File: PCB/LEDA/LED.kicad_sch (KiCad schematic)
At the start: 25 parts, among them J1 USB_A, J2 Conn_01x03, J3 TC2030-USB-NL-DS, U1 ICS43434_MEMS_Mic, U2 ESP32-S3-MINI-1, U5 MD8942

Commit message: PCB Update
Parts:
- C4, C6: LCSC Part # C194427 -> (none); MPN (none) -> C194427
- C7: LCSC Part # C1691 -> (none); MPN (none) -> C1691
- D1: LCSC Part # C5349953 -> (none); MPN (none) -> C5349953
- D2: LCSC Part # C5137770 -> (none); MPN (none) -> C5137770
- J2: LCSC Part # C2765056 -> (none); MPN (none) -> C2765056
- U1: LCSC Part # C5656610 -> (none); MPN (none) -> C5656610
- U2: LCSC Part # C3013941 -> (none); MPN (none) -> C3013941
- U5: LCSC Part # C2684786 -> (none); MPN (none) -> C2684786
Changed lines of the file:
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@@
 			)
 		)
-		(property "LCSC Part #" "C1691"
+		(property "MPN" "C1691"
 			(at 254.635 41.275 0)
 			(effects
@@
 			)
 		)
-		(property "LCSC Part #" "C2684786"
+		(property "MPN" "C2684786"
 			(at 233.68 72.39 0)
 			(effects
@@
 			)
 		)
-		(property "LCSC Part #" "C194427"
+		(property "MPN" "C194427"
 			(at 254.635 39.37 0)
 			(effects
@@
 			)
 		)
-		(property "LCSC Part #" "C5349953"
+		(property "MPN" "C5349953"
 			(at 164.465 85.725 0)
 			(effects
@@
 			)
 		)
-		(property "LCSC Part #" "C194427"
+		(property "MPN" "C194427"
 			(at 160.655 32.385 0)
 			(effects
@@
 			)
 		)
-		(property "LCSC Part #" "C5656610"
+		(property "MPN" "C5656610"
 			(at 196.215 75.438 0)
 			(effects
@@
 			)
 		)
-		(property "LCSC Part #" "C5137770"
+		(property "MPN" "C5137770"
 			(at 181.61 97.155 0)
 			(effects
@@
 			)
 		)
-		(property "LCSC Part #" "C3013941"
+		(property "MPN" "C3013941"
 			(at 109.22 111.76 0)
 			(effects
@@
 			)
 		)
-		(property "LCSC Part #" "C2765056"
+		(property "MPN" "C2765056"
 			(at 201.295 97.155 0)
 			(effects

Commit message: Latest layout
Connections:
- net D-: now also J3.2 (NC), J3.6 (NC)
- net DC: no longer J3.2 (VBUS)
- net GND: no longer J3.6 (GND)
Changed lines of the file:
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@@
 (kicad_sch
-	(version 20231120)
+	(version 20241209)
 	(generator "eeschema")
-	(generator_version "8.0")
+	(generator_version "9.0")
 	(paper "A4")
 	(title_block
@@
 			)
 		)
-		(property "Datasheet" " ~"
+		(property "Datasheet" "~"
 			(at 237.49 80.645 0)
 			(effects
@@
 		)
 	)
+	(embedded_fonts no)
 )

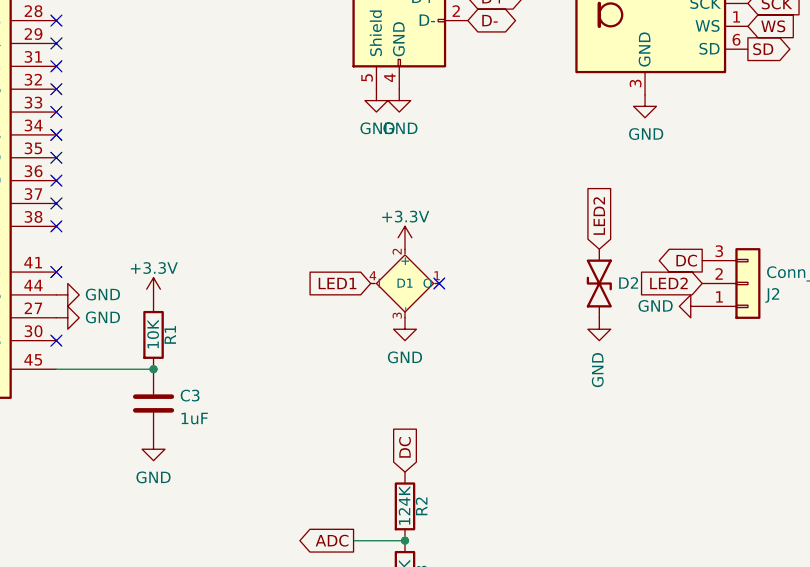
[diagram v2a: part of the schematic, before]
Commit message: New LEDs
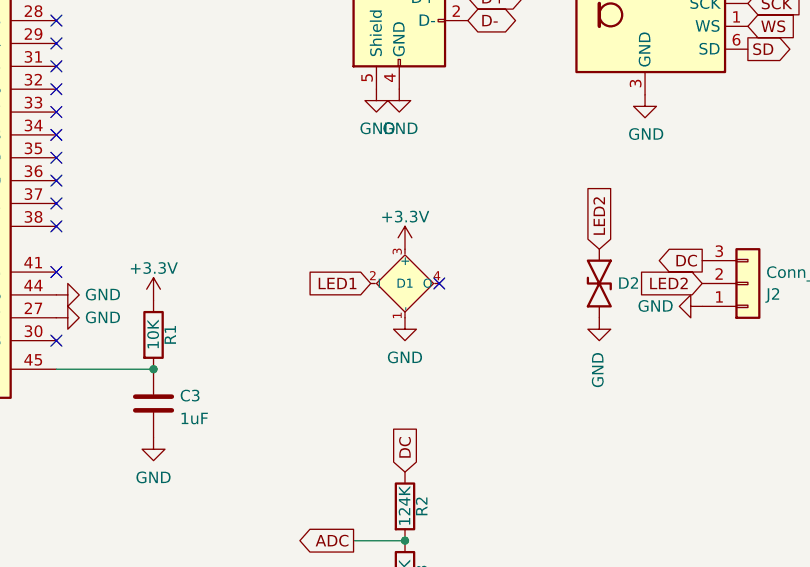
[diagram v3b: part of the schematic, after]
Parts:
- D1: footprint RevK:SMD1010 -> RevK:SMD1615; symbol RevK:WS2812B-1mm -> RevK:WS2812B-1.5mm; MPN C5349953 -> C5349954
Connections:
- net +3.3V: now also D1.3 (+); no longer D1.2 (+)
- net GND: now also D1.1 (-); no longer D1.3 (-)
- net LED1: now also D1.2 (I); no longer D1.4 (I)
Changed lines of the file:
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@@
 (kicad_sch
-	(version 20241209)
+	(version 20250114)
 	(generator "eeschema")
 	(generator_version "9.0")
@@
 	)
 	(symbol
-		(lib_id "RevK:WS2812B-1mm")
+		(lib_id "RevK:WS2812B-1.5mm")
 		(at 163.195 97.155 0)
-		(mirror x)
 		(unit 1)
 		(exclude_from_sim no)
@@
 		)
 		(property "Value" "XL-1010RGBC-WS2812B"
-			(at 164.465 91.44 0)
+			(at 164.465 102.87 0)
 			(effects
 				(font
@@
 			)
 		)
-		(property "Footprint" "RevK:SMD1010"
+		(property "Footprint" "RevK:SMD1615"
 			(at 164.465 89.535 0)
 			(effects
@@
 			)
 		)
-		(property "Datasheet" "https://datasheet.lcsc.com/lcsc/2301111010_XINGLIGHT-XL-1010RGBC-WS2812B_C5349953.pdf"
+		(property "Datasheet" "https://www.lcsc.com/datasheet/C5349954.pdf"
 			(at 164.465 87.63 0)
 			(effects
@@
 			)
 		)
-		(property "MPN" "C5349953"
+		(property "MPN" "C5349954"
 			(at 164.465 85.725 0)
 			(effects

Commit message: Not a good case, but started one, and some cleaner renders
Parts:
- J2: footprint RevK:WAGO-2060-453-998-404 -> RevK:WAGO-2060-453-998-404-O
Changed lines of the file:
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@@
 			)
 		)
-		(property "Footprint" "RevK:WAGO-2060-453-998-404"
+		(property "Footprint" "RevK:WAGO-2060-453-998-404-O"
 			(at 201.295 97.155 0)
 			(effects
